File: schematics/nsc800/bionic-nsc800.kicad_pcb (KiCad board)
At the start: 2 copper layers, 48.3 x 71.1 mm, 10 parts, among them J1 Bionic-P135, J2 Bionic-P245, U1 NSC800N, U2 74HCT126, U3 11AA010-I/TO

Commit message: [NSC800] Update schematics
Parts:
- removed MH1, MH2, MH3, MH4: MountingHole_3.2mm_M3, MountingHole:MountingHole_3.2mm_M3
- removed U3: 11AA010-I/TO, microchip:TO-92_MC_MCH
- added C2: 22u, Capacitor_SMD:C_0603_1608Metric_Pad1.08x0.95mm_HandSolder, B.Cu at (123.9, 74.2)
- added D1: CSL1901UW1, 0-LocalLibrary:LED_CSL1901UW1_ROM, F.Cu at (113.7, 71.8)
- added R1: 1.6k, Resistor_SMD:R_0603_1608Metric_Pad0.98x0.95mm_HandSolder, F.Cu at (109.9, 71.8)
- C1: footprint Capacitor_THT:C_Disc_D3.4mm_W2.1mm_P2.50mm -> Capacitor_SMD:C_0603_1608Metric_Pad1.08x0.95mm_HandSolder
- J1: footprint connector:Bionic-P135_Vertical -> 0-LocalLibrary:Bionic-P135_Vertical; moved to B.Cu
- J2: footprint connector:Bionic-P245_Vertical -> 0-LocalLibrary:Bionic-P245_Vertical; moved to B.Cu
- U1: footprint Package_DIP:DIP-40_W15.24mm -> 0-LocalLibrary:DIP-40_W15.24mm_Socket
- U2: value 74HCT126 -> 11AA010-I/TT; footprint Package_DIP:DIP-14_W7.62mm -> 0-LocalLibrary:SOT-23_MC_MCH-M
- moved C1 57.1 mm to (123.9, 74.2), turned to 90 degrees
- moved U1 17.8 mm to (106.1, 75.1)
- moved U2 12.0 mm to (113.7, 129.6), turned to 180 degrees
- moved J2 6.35 mm to (117.5, 75.1), turned to 180 degrees
- moved J1 6.35 mm to (109.9, 75.1), turned to 180 degrees
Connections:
- J2 pad 37: unconnected-(J2-P41-Pad37) -> /P41
- U1 pad 11: Net-(U1-XIN) -> /P50
- U1 pad 21: /P43 -> /P35
- U1 pad 22: /P30 -> /P32
- U1 pad 24: /P32 -> /P30
- U1 pad 25: /P42 -> /P34
- U1 pad 26: /P54 -> /P46
- U1 pad 27: /P35 -> /P41
- U1 pad 29: /P34 -> /P40
- U1 pad 30: /P40 -> /P54
- U1 pad 31: /P51 -> /P43
- U1 pad 32: /P50 -> /P42
- U1 pad 33: Net-(U1-~{RESETIN}) -> /P53
- U1 pad 37: unconnected-(U1-RESETO-Pad37) -> /P51
- U2 pad 1: VCC -> Net-(J2-P57)
- U2 pad 2: /P46 -> VCC
- U2 pad 3: Net-(U1-XIN) -> GND
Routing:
- net VCC: track 0.00 -> 89.5 mm
- net /P52: track 0.00 -> 57.1 mm
- net /P51: track 0.00 -> 56.4 mm, vias 0 -> 1
- net /P53: track 0.00 -> 49.8 mm
- net /P37: track 0.00 -> 40.1 mm, vias 0 -> 1
- net /P55: track 0.00 -> 39.6 mm
- net /P44: track 0.00 -> 34.6 mm
- net /P36: track 0.00 -> 34.3 mm, vias 0 -> 1
- net /P13: track 0.00 -> 31.4 mm, vias 0 -> 1
- net /P12: track 0.00 -> 31.3 mm, vias 0 -> 1
- net /P11: track 0.00 -> 30.9 mm, vias 0 -> 1
- net /P14: track 0.00 -> 30.6 mm, vias 0 -> 1
- net /P15: track 0.00 -> 30.2 mm
- net /P10: track 0.00 -> 30.2 mm
- net /P47: track 0.00 -> 30.2 mm, vias 0 -> 1
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- added copper zone on B.Cu, net GND
- added copper zone on F.Cu, net GND
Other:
- board size 48.3 x 71.1 mm -> 25.4 x 68.6 mm
- board text added: "BionicNSC800"
- board text added: "JLCJLCJLCJLC"
- board text added: "Rev. 3"

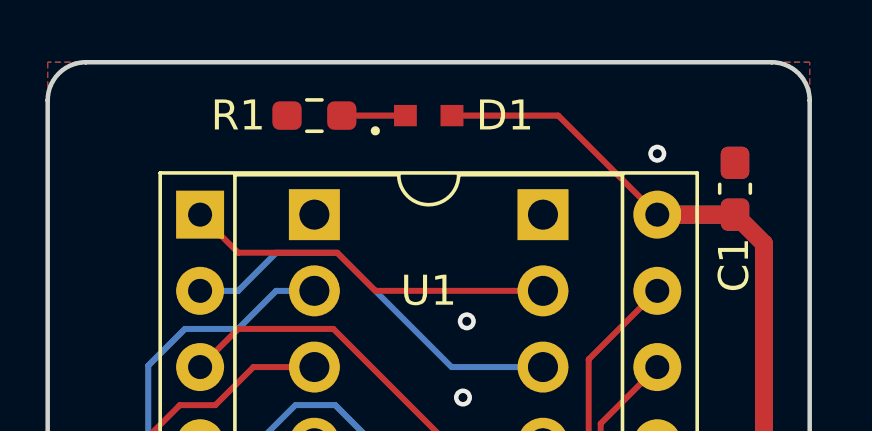
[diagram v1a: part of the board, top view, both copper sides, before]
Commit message: [schematics] Update LED footprint
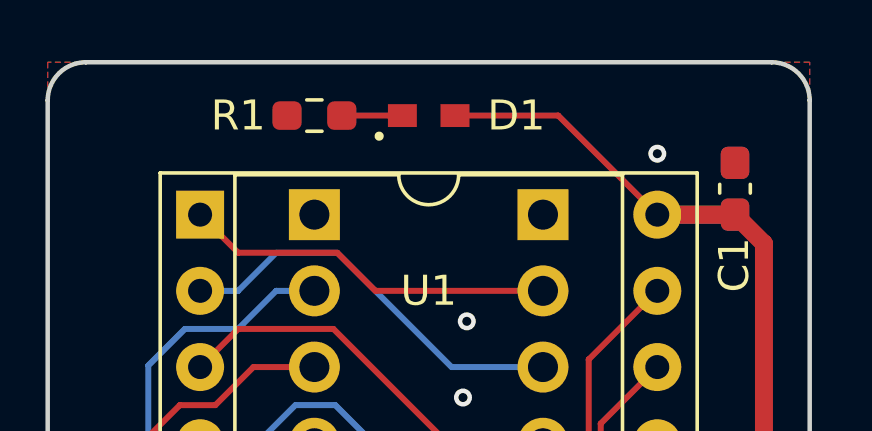
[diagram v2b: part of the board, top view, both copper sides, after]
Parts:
- D1: footprint 0-LocalLibrary:LED_CSL1901UW1_ROM -> 0-LocalLibrary:LED_CSL1901UW1_ROM-M

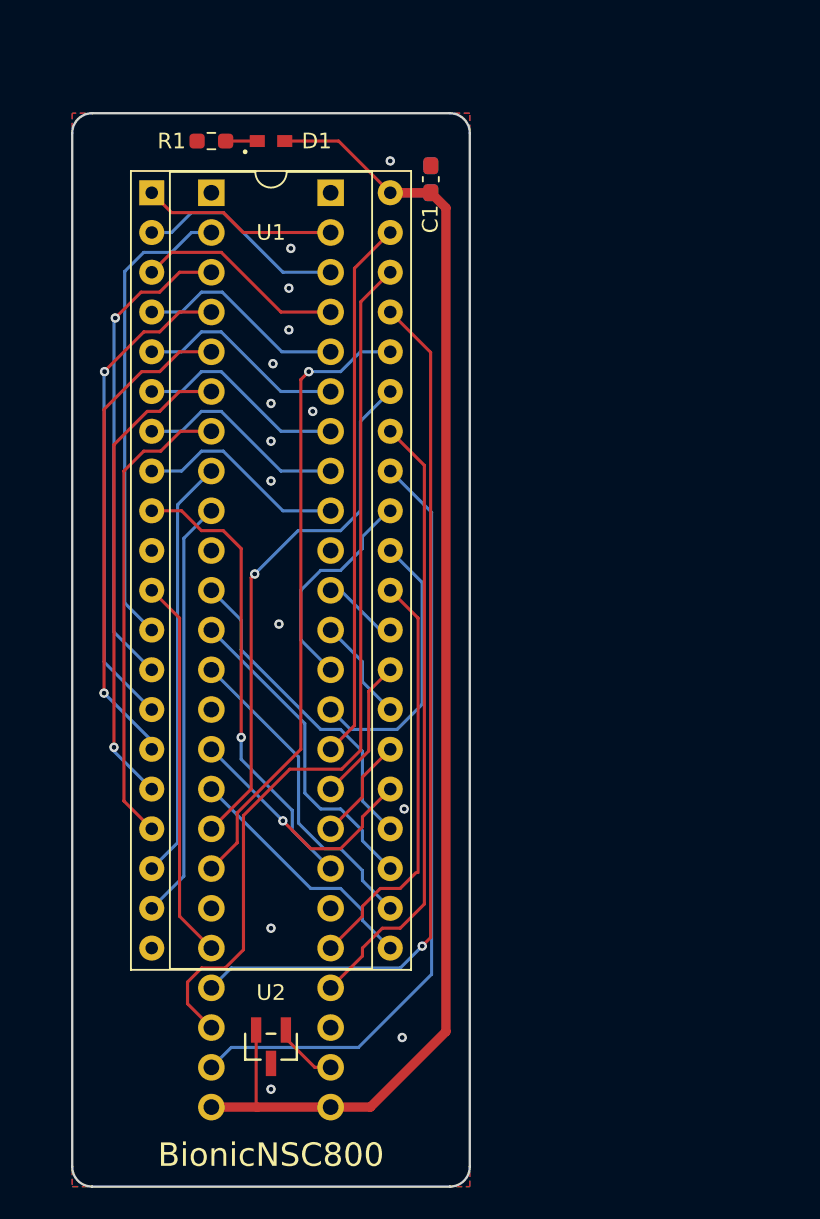
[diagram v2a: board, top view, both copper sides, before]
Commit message: [NSC800] Cleanup schematics
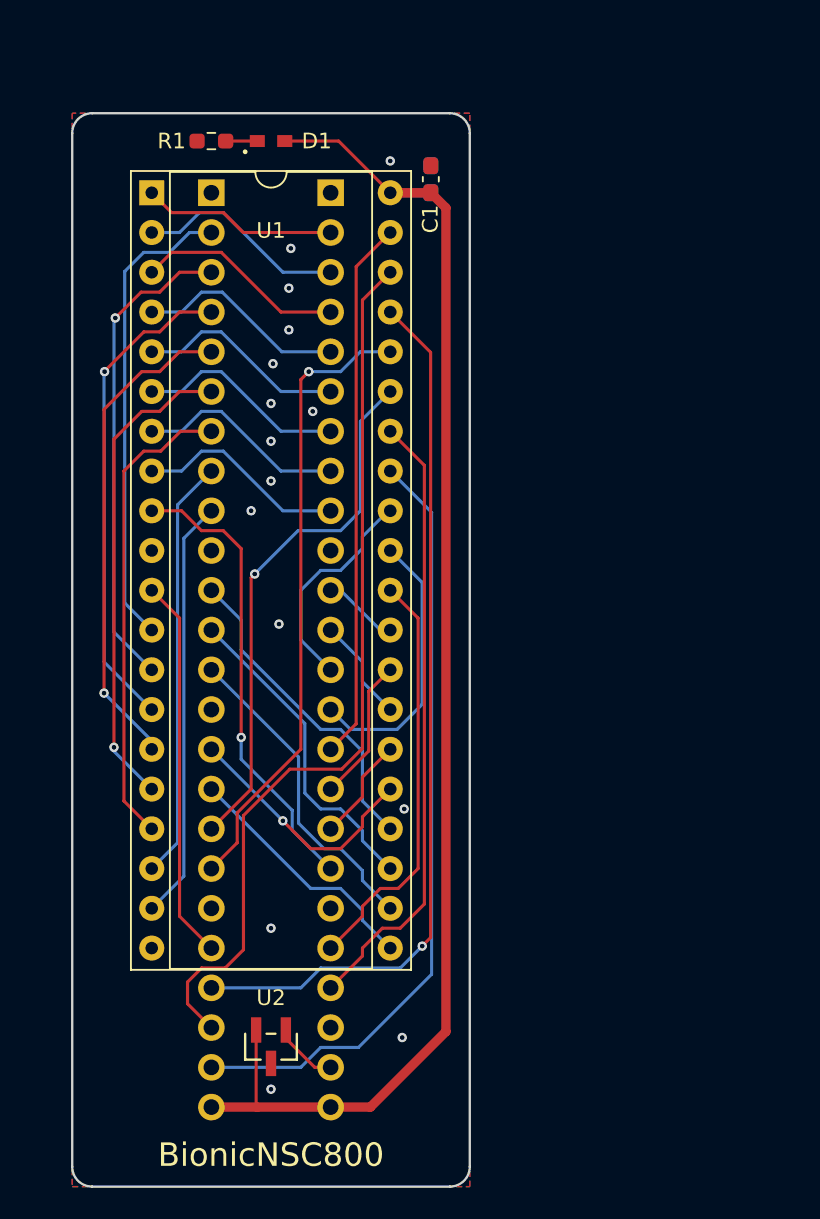
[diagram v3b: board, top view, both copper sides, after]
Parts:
- D1: footprint 0-LocalLibrary:LED_CSL1901UW1_ROM-M -> rhom:LED_CSL1901UW1_ROM-M
- J1: footprint 0-LocalLibrary:Bionic-P135_Vertical -> bionic:Bionic-P135_Vertical
- J2: footprint 0-LocalLibrary:Bionic-P245_Vertical -> bionic:Bionic-P245_Vertical
- U1: footprint 0-LocalLibrary:DIP-40_W15.24mm_Socket -> bionic:DIP-40_W15.24mm_Socket
- U2: footprint 0-LocalLibrary:SOT-23_MC_MCH-M -> microchip:SOT-23_MC_MCH-M
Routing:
- net GND: vias 14 -> 15
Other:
- rule pad_to_mask_clearance: 0.051 -> 0

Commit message: [NSC800] Update schematics
Remove unused pins from bionic connector
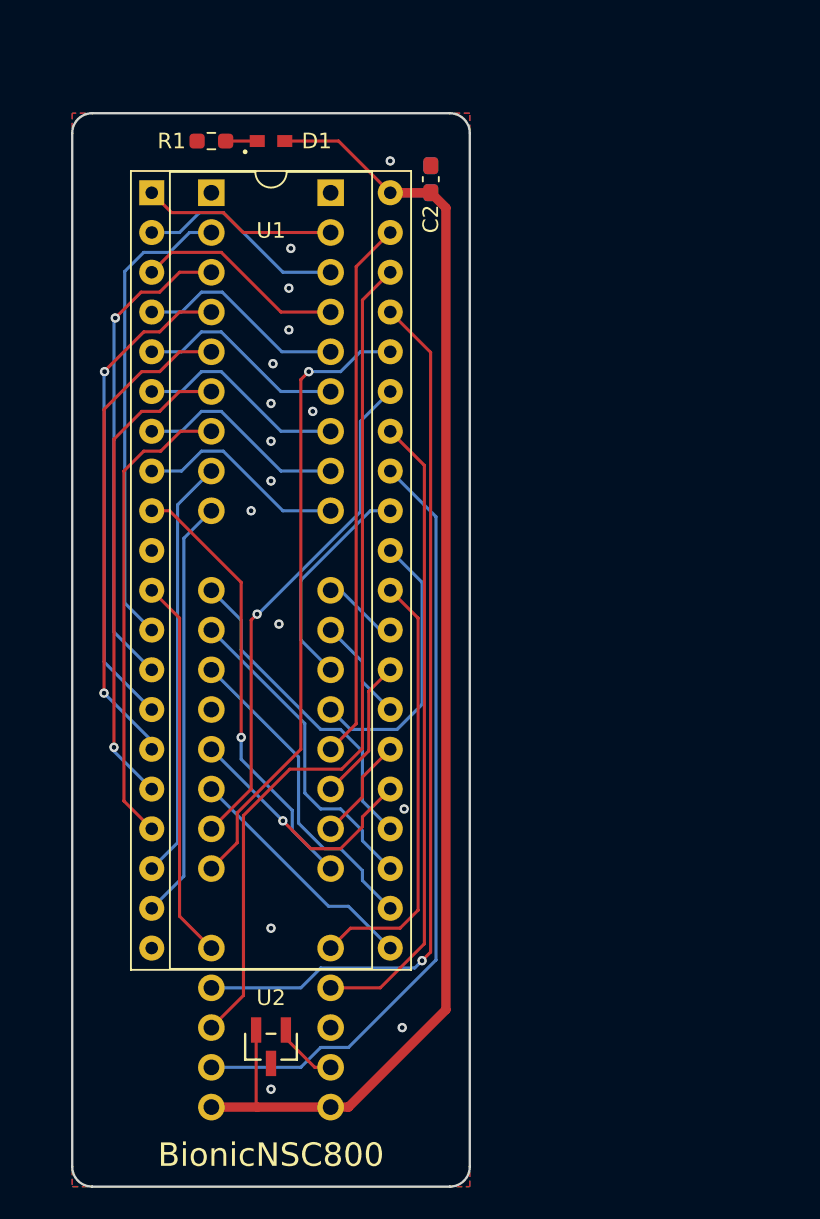
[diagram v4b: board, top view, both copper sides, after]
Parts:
- C1: moved to B.Cu
- C2: moved to F.Cu
- J1: footprint bionic:Bionic-P135_Vertical -> bionic:Bionic-P135_THT
- J2: footprint bionic:Bionic-P245_Vertical -> bionic:Bionic-P245_THT
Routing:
- net /P52: track 57.1 -> 54.9 mm
- net /P36: track 34.3 -> 32.7 mm
- net /P47: track 30.2 -> 28.9 mm
- net /P55: track 39.6 -> 40.8 mm
- net /P54: track 26.6 -> 27.8 mm
- net VCC: track 89.4 -> 88.5 mm
- net /P51: track 56.4 -> 56.9 mm
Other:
- board text added: "Rev. 4"
- board text removed: "Rev. 3"
